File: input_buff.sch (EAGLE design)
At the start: 37 parts, among them X1 057-010-1, X2 057-016-1

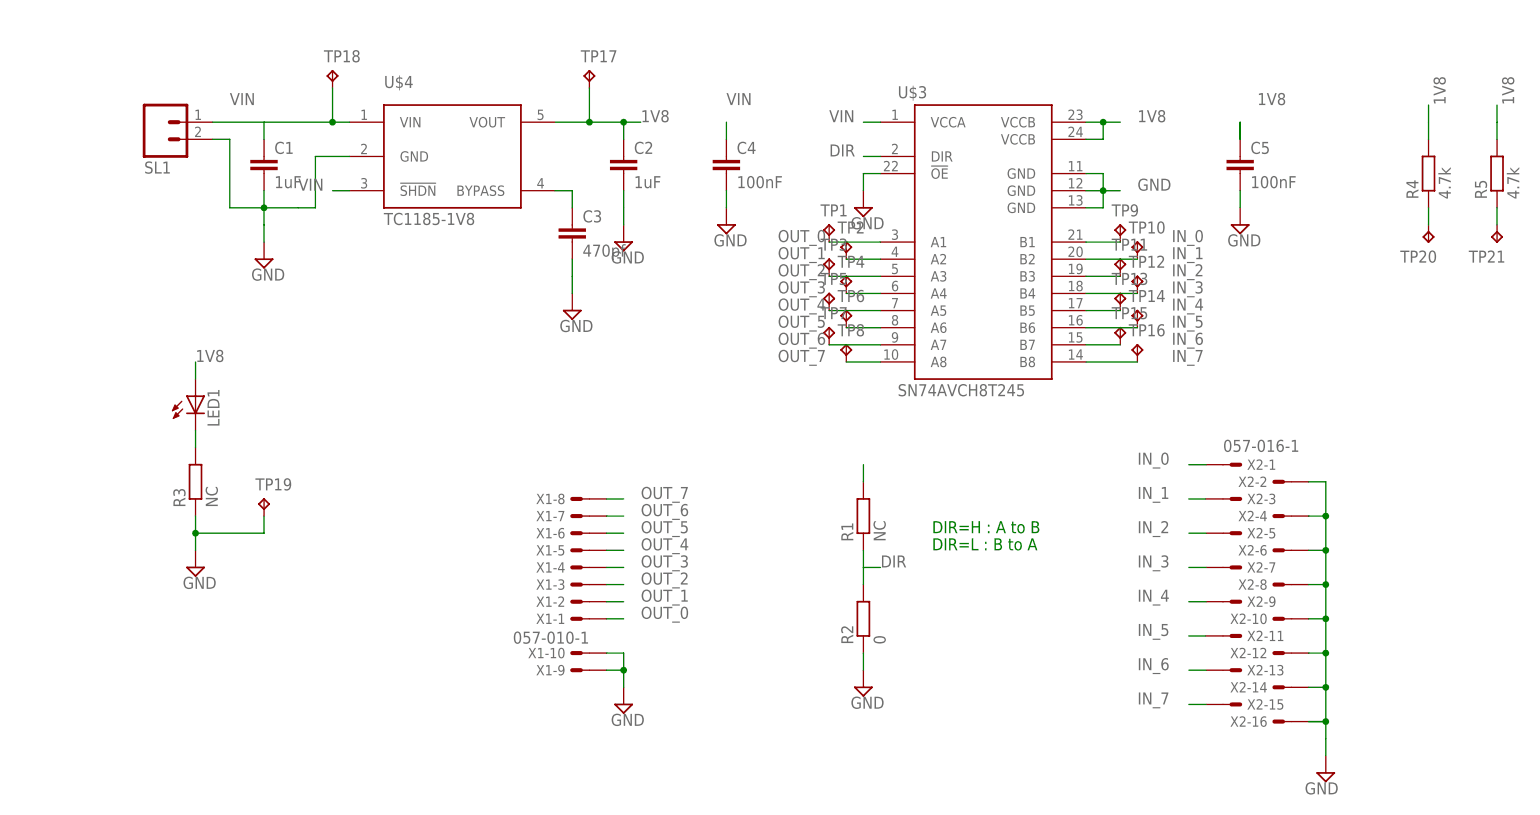
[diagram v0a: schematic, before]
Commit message: change led to cms, add addtionnal capa place
add an addtionnal 1206 capa before ldo
change led to 0805 smd
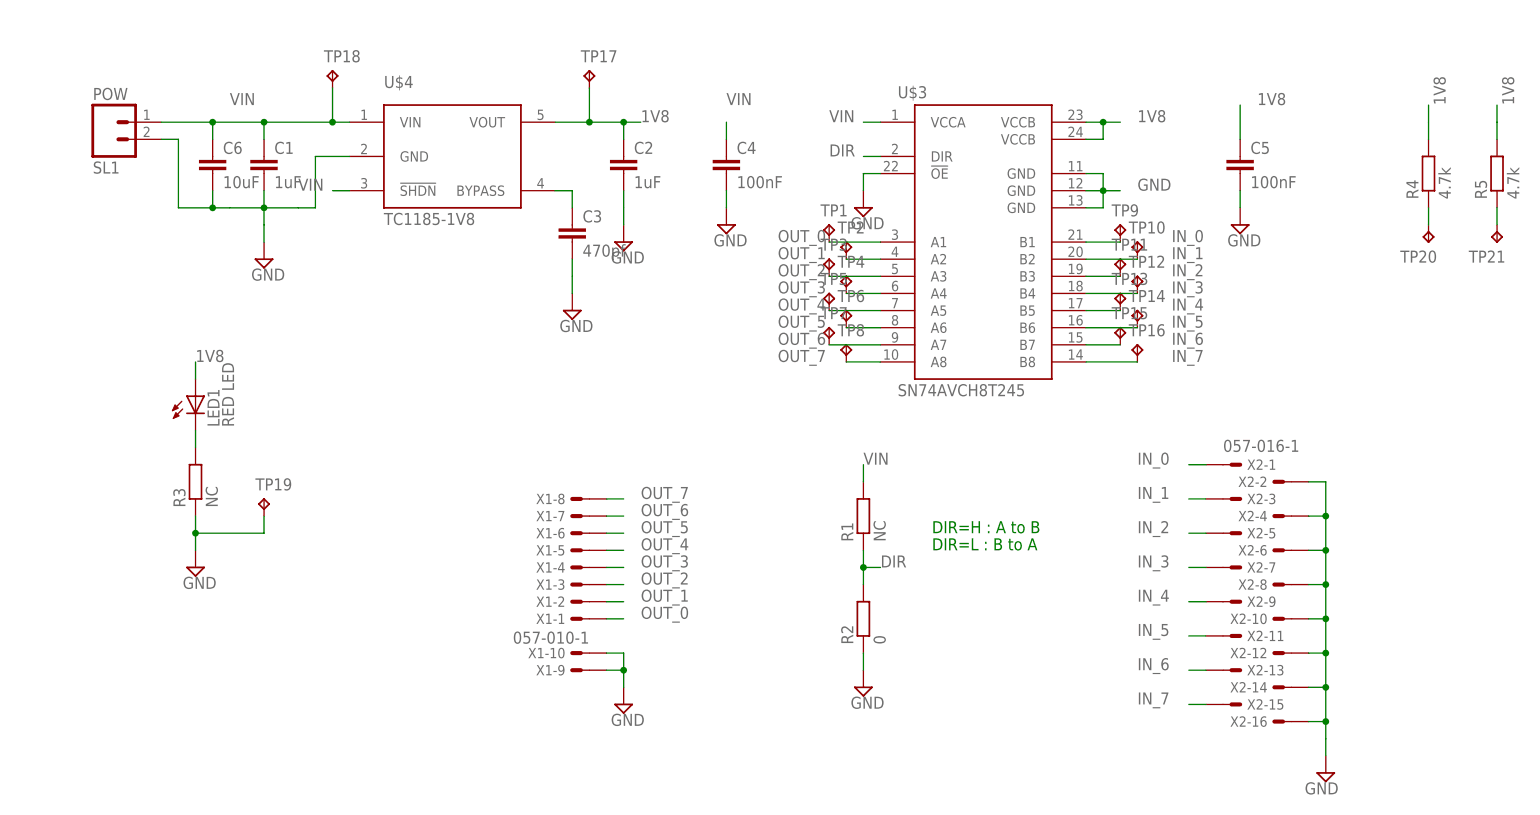
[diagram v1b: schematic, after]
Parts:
- added C6: 10uF, resistor:C-EUC1210
- LED1: value (none) -> RED LED; device led:LED3MM -> led:LEDCHIPLED_0805
- SL1: value (none) -> POW
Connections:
- net GND: now also C6.2
- net VIN: now also C6.1
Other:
- moved on the sheet: SL1

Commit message: final design + matching gerbers (production files)
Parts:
- removed SL1: POW, con-amp-quick:M02
- added R6: 4.7k, resistor:R-EU_M0805
- added SL2: POW, con-amp-quick:M02
- added X3: 22-23-2021, con-molex:22-23-2021
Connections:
- new net !OE: R6.2, SL2.2, U$3.!OE
- net GND: now also R6.1, X3-1.S; no longer SL1.2, U$3.!OE
- net VIN: now also SL2.1, X3-2.S; no longer SL1.1
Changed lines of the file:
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@@
 <?xml version="1.0" encoding="utf-8"?>
 <!DOCTYPE eagle SYSTEM "eagle.dtd">
-<eagle version="6.1">
+<eagle version="6.0">
 <drawing>
 <settings>
@@
 <part name="SUPPLY4" library="supply2" deviceset="GND" device=""/>
 <part name="SUPPLY5" library="supply2" deviceset="GND" device=""/>
-<part name="SUPPLY6" library="supply2" deviceset="GND" device=""/>
 <part name="X1" library="con-panduit" deviceset="057-010-" device="1"/>
 <part name="X2" library="con-panduit" deviceset="057-016-" device="1"/>
 <part name="SUPPLY7" library="supply2" deviceset="GND" device=""/>
 <part name="SUPPLY8" library="supply2" deviceset="GND" device=""/>
-<part name="SL1" library="con-amp-quick" deviceset="M02" device="" value="POW"/>
 <part name="TP17" library="testpad" deviceset="TP" device="TP10R">
 <attribute name="TP_SIGNAL_NAME" value=""/>
@@
 <part name="C6" library="resistor" deviceset="C-EU" device="C1210" value="10uF"/>
 <part name="LED1" library="led" deviceset="LED" device="CHIPLED_0805" value="RED LED"/>
+<part name="R6" library="resistor" deviceset="R-EU_" device="M0805" value="4.7k"/>
+<part name="SUPPLY6" library="supply2" deviceset="GND" device=""/>
+<part name="SL2" library="con-amp-quick" deviceset="M02" device="" value="POW">
+<attribute name="MF" value=""/>
+<attribute name="MPN" value=""/>
+<attribute name="OC_FARNELL" value="unknown"/>
+<attribute name="OC_NEWARK" value="unknown"/>
+</part>
+<part name="X3" library="con-molex" deviceset="22-23-2021" device=""/>
 </parts>
 <sheets>
@@
 <instance part="SUPPLY4" gate="GND" x="88.9" y="15.24"/>
 <instance part="SUPPLY5" gate="GND" x="165.1" y="15.24"/>
-<instance part="SUPPLY6" gate="GND" x="109.22" y="17.78"/>
 <instance part="X1" gate="-1" x="66.04" y="-43.18" rot="R180"/>
 <instance part="X1" gate="-2" x="66.04" y="-40.64" rot="R180"/>
@@
 <instance part="SUPPLY7" gate="GND" x="177.8" y="-66.04" rot="MR0"/>
 <instance part="SUPPLY8" gate="GND" x="73.66" y="-55.88"/>
-<instance part="SL1" gate="G$1" x="-2.54" y="30.48" rot="MR180"/>
 <instance part="TP17" gate="G$1" x="68.58" y="38.1"/>
 <instance part="TP18" gate="G$1" x="30.48" y="38.1"/>
@@
 <instance part="C6" gate="G$1" x="12.7" y="25.4"/>
 <instance part="LED1" gate="G$1" x="10.16" y="-10.16"/>
+<instance part="R6" gate="G$1" x="182.88" y="22.86" rot="R90"/>
+<instance part="SUPPLY6" gate="GND" x="182.88" y="12.7"/>
+<instance part="SL2" gate="G$1" x="175.26" y="40.64" rot="MR180"/>
+<instance part="X3" gate="-1" x="0" y="27.94" rot="R180"/>
+<instance part="X3" gate="-2" x="0" y="30.48" rot="R180"/>
 </instances>
 <busses>
@@
 <wire x1="20.32" y1="30.48" x2="30.48" y2="30.48" width="0.1524" layer="91"/>
 <label x="15.24" y="33.02" size="1.778" layer="95"/>
-<pinref part="SL1" gate="G$1" pin="1"/>
 <wire x1="30.48" y1="30.48" x2="33.02" y2="30.48" width="0.1524" layer="91"/>
 <wire x1="5.08" y1="30.48" x2="12.7" y2="30.48" width="0.1524" layer="91"/>
@@
 <junction x="12.7" y="30.48"/>
 <junction x="20.32" y="30.48"/>
+<pinref part="X3" gate="-2" pin="S"/>
+<wire x1="5.08" y1="30.48" x2="2.54" y2="30.48" width="0.1524" layer="91"/>
 </segment>
 <segment>
@@
 <wire x1="109.22" y1="-22.86" x2="109.22" y2="-20.32" width="0.1524" layer="91"/>
 <label x="109.22" y="-20.32" size="1.778" layer="95"/>
+</segment>
+<segment>
+<pinref part="SL2" gate="G$1" pin="1"/>
+<wire x1="182.88" y1="40.64" x2="185.42" y2="40.64" width="0.1524" layer="91"/>
+<wire x1="185.42" y1="40.64" x2="185.42" y2="43.18" width="0.1524" layer="91"/>
 </segment>
 </net>
@@
 <junction x="20.32" y="17.78"/>
 <wire x1="15.24" y1="17.78" x2="12.7" y2="17.78" width="0.1524" layer="91"/>
-<pinref part="SL1" gate="G$1" pin="2"/>
 <wire x1="12.7" y1="17.78" x2="7.62" y2="17.78" width="0.1524" layer="91"/>
 <wire x1="5.08" y1="27.94" x2="7.62" y2="27.94" width="0.1524" layer="91"/>
@@
 <wire x1="12.7" y1="17.78" x2="12.7" y2="20.32" width="0.1524" layer="91"/>
 <junction x="12.7" y="17.78"/>
+<pinref part="X3" gate="-1" pin="S"/>
+<wire x1="5.08" y1="27.94" x2="2.54" y2="27.94" width="0.1524" layer="91"/>
 </segment>
 <segment>
@@
 <wire x1="88.9" y1="20.32" x2="88.9" y2="17.78" width="0.1524" layer="91"/>
 <pinref part="SUPPLY4" gate="GND" pin="GND"/>
-</segment>
-<segment>
-<pinref part="U$3" gate="G$1" pin="!OE"/>
-<pinref part="SUPPLY6" gate="GND" pin="GND"/>
-<wire x1="111.76" y1="22.86" x2="109.22" y2="22.86" width="0.1524" layer="91"/>
-<wire x1="109.22" y1="22.86" x2="109.22" y2="20.32" width="0.1524" layer="91"/>
 </segment>
 <segment>
@@
 <junction x="10.16" y="-30.48"/>
 </segment>
+<segment>
+<pinref part="SUPPLY6" gate="GND" pin="GND"/>
+<pinref part="R6" gate="G$1" pin="1"/>
+<wire x1="182.88" y1="15.24" x2="182.88" y2="17.78" width="0.1524" layer="91"/>
+</segment>
 </net>
 <net name="OUT_0" class="0">
@@
 </segment>
 </net>
+<net name="!OE" class="0">
+<segment>
+<pinref part="U$3" gate="G$1" pin="!OE"/>
+<wire x1="111.76" y1="22.86" x2="109.22" y2="22.86" width="0.1524" layer="91"/>
+<label x="104.14" y="22.86" size="1.778" layer="95"/>
+</segment>
+<segment>
+<pinref part="R6" gate="G$1" pin="2"/>
+<wire x1="182.88" y1="27.94" x2="182.88" y2="33.02" width="0.1524" layer="91"/>
+<label x="185.42" y="33.02" size="1.778" layer="95"/>
+<wire x1="182.88" y1="33.02" x2="185.42" y2="33.02" width="0.1524" layer="91"/>
+<wire x1="185.42" y1="33.02" x2="182.88" y2="33.02" width="0.1524" layer="91"/>
+<wire x1="182.88" y1="33.02" x2="182.88" y2="35.56" width="0.1524" layer="91"/>
+<junction x="182.88" y="33.02"/>
+<pinref part="SL2" gate="G$1" pin="2"/>
+<wire x1="182.88" y1="38.1" x2="185.42" y2="38.1" width="0.1524" layer="91"/>
+<wire x1="185.42" y1="38.1" x2="185.42" y2="35.56" width="0.1524" layer="91"/>
+<wire x1="185.42" y1="35.56" x2="182.88" y2="35.56" width="0.1524" layer="91"/>
+</segment>
+</net>
